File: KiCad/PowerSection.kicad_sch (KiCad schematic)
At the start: 24 parts, among them U2 LM7805_TO220, U4 LM337_TO220, U6 MC34063AP, U7 LM7810_TO220

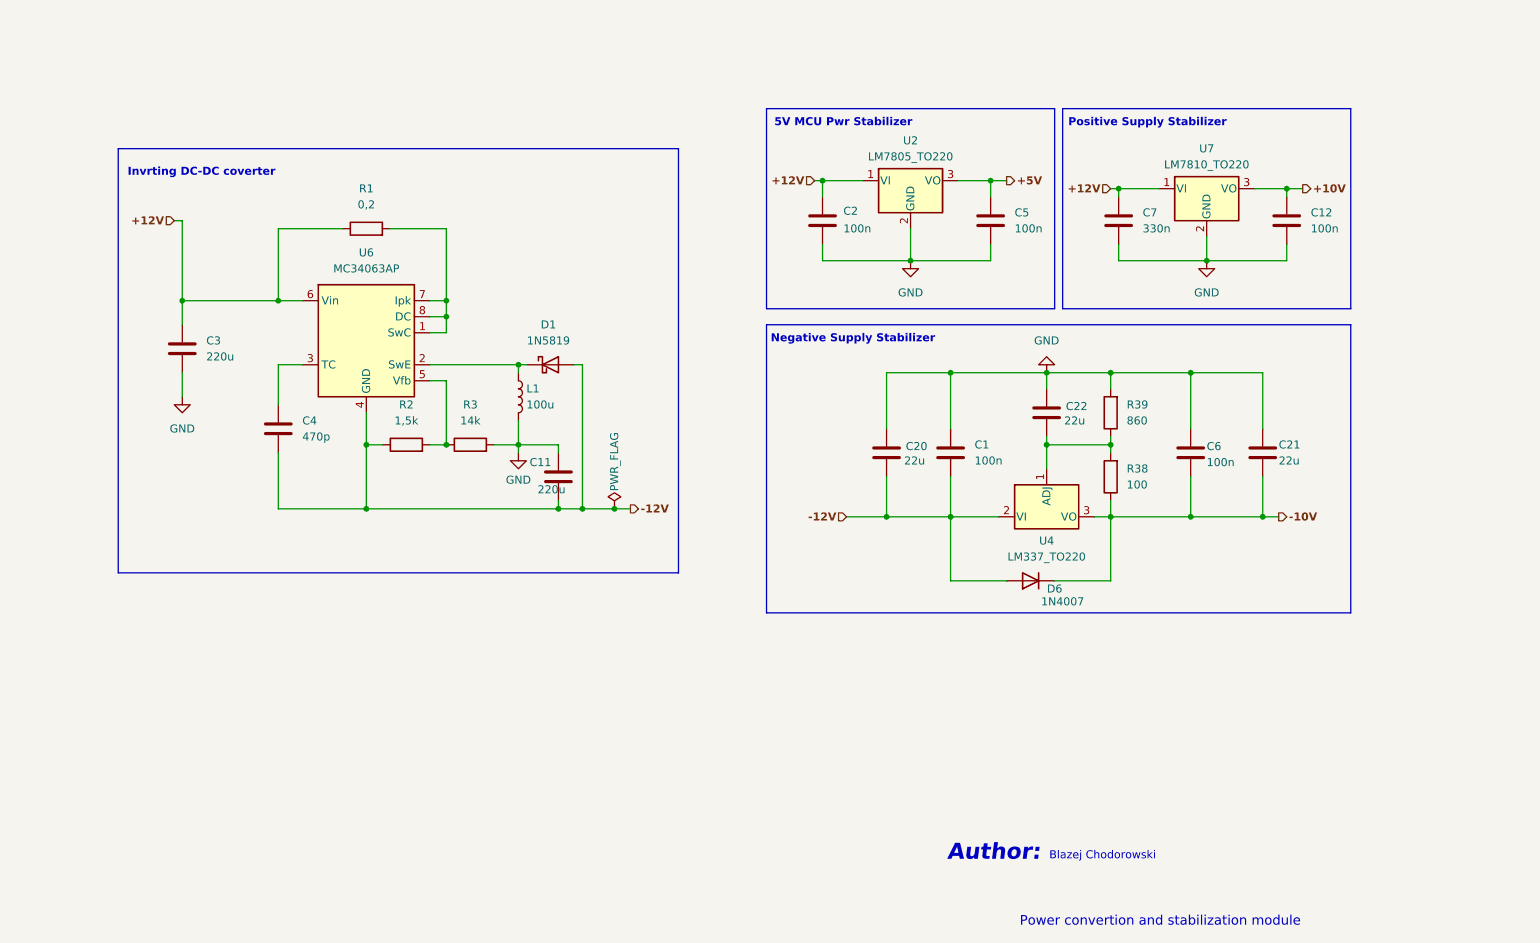
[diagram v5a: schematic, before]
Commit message: First DAC layout, rough board layout
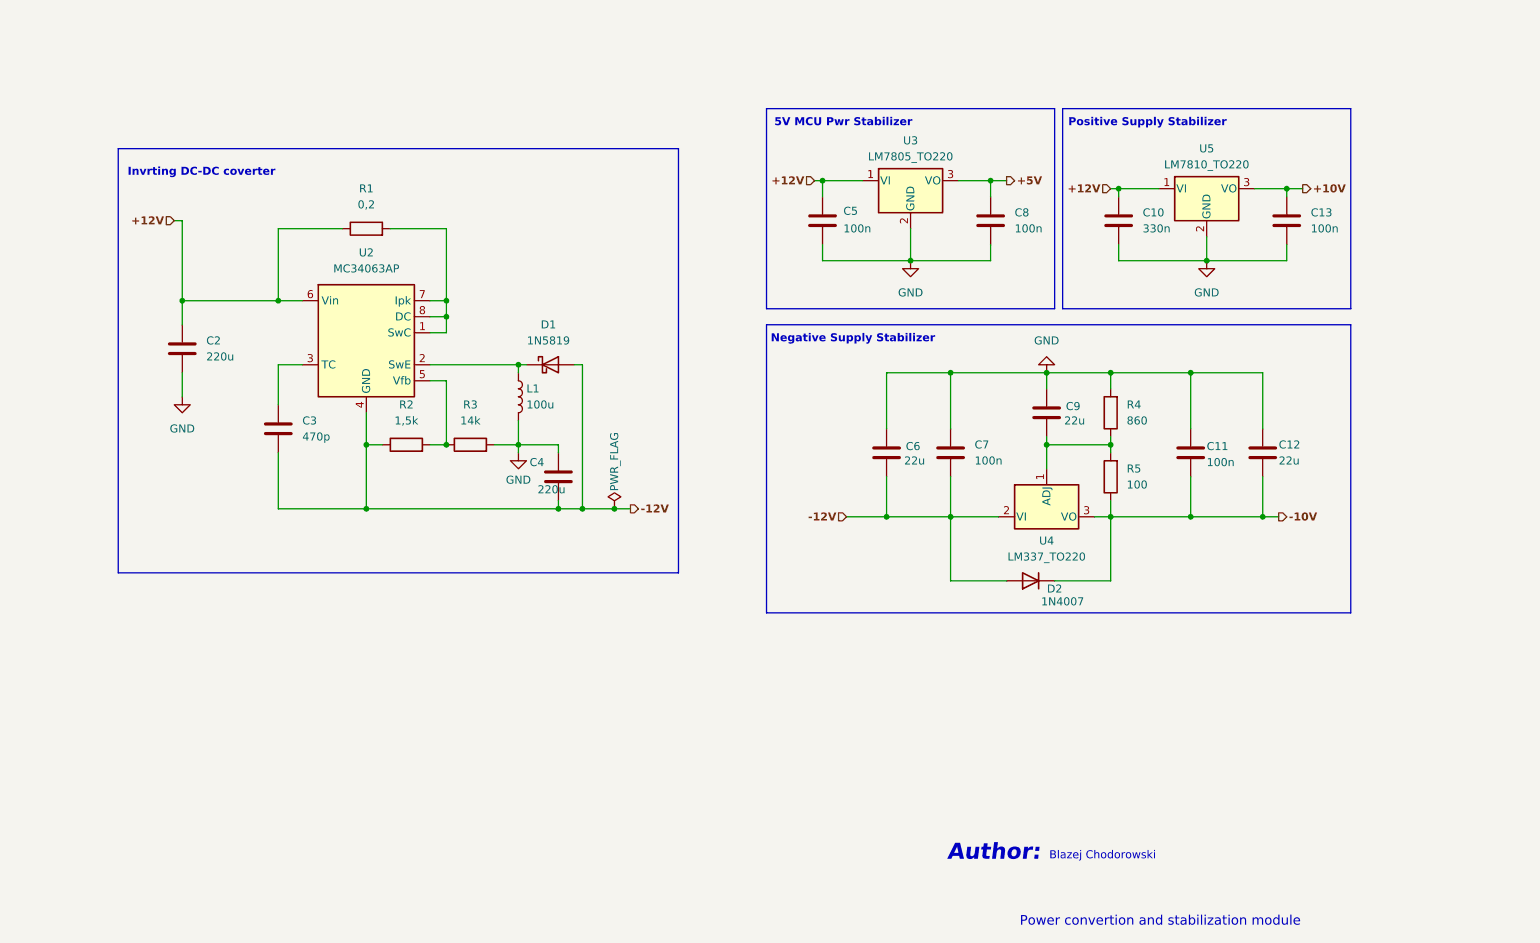
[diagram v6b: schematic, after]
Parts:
- renumbered C7 to C10, C6 to C11, C21 to C12, C12 to C13, C3 to C2, C4 to C3, C11 to C4, C2 to C5, C20 to C6, C1 to C7, C5 to C8, C22 to C9, D6 to D2, R39 to R4, R38 to R5, U6 to U2, U2 to U3, U7 to U5
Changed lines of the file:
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@@
 		(on_board yes)
 		(dnp no)
-		(property "Reference" "C6"
+		(property "Reference" "C11"
 			(at 218.44 114.554 0)
 			(effects
@@
 			(project "SiganlGen"
 				(path "/e2db369b-fed9-4358-b449-15db5155edf2/27026b69-1c54-41be-a6f6-95a262163c29"
-					(reference "C6")
+					(reference "C11")
 					(unit 1)
 				)
@@
 		(dnp no)
 		(fields_autoplaced yes)
-		(property "Reference" "C1"
+		(property "Reference" "C7"
 			(at 181.61 114.2999 0)
 			(effects
@@
 			(project "SiganlGen"
 				(path "/e2db369b-fed9-4358-b449-15db5155edf2/27026b69-1c54-41be-a6f6-95a262163c29"
-					(reference "C1")
+					(reference "C7")
 					(unit 1)
 				)
@@
 		(dnp no)
 		(fields_autoplaced yes)
-		(property "Reference" "R38"
+		(property "Reference" "R5"
 			(at 205.74 118.1099 0)
 			(effects
@@
 			(project "SiganlGen"
 				(path "/e2db369b-fed9-4358-b449-15db5155edf2/27026b69-1c54-41be-a6f6-95a262163c29"
-					(reference "R38")
+					(reference "R5")
 					(unit 1)
 				)
@@
 		(dnp no)
 		(fields_autoplaced yes)
-		(property "Reference" "R39"
+		(property "Reference" "R4"
 			(at 205.74 107.9499 0)
 			(effects
@@
 			(project "SiganlGen"
 				(path "/e2db369b-fed9-4358-b449-15db5155edf2/27026b69-1c54-41be-a6f6-95a262163c29"
-					(reference "R39")
+					(reference "R4")
 					(unit 1)
 				)
@@
 		(dnp no)
 		(fields_autoplaced yes)
-		(property "Reference" "C4"
+		(property "Reference" "C3"
 			(at 74.93 110.4899 0)
 			(effects
@@
 			(project "SiganlGen"
 				(path "/e2db369b-fed9-4358-b449-15db5155edf2/27026b69-1c54-41be-a6f6-95a262163c29"
-					(reference "C4")
+					(reference "C3")
 					(unit 1)
 				)
@@
 		(dnp no)
 		(fields_autoplaced yes)
-		(property "Reference" "U6"
+		(property "Reference" "U2"
 			(at 85.09 83.82 0)
 			(effects
@@
 			(project "SiganlGen"
 				(path "/e2db369b-fed9-4358-b449-15db5155edf2/27026b69-1c54-41be-a6f6-95a262163c29"
-					(reference "U6")
+					(reference "U2")
 					(unit 1)
 				)
@@
 		(dnp no)
 		(fields_autoplaced yes)
-		(property "Reference" "C7"
+		(property "Reference" "C10"
 			(at 208.28 77.4699 0)
 			(effects
@@
 			(project "SiganlGen"
 				(path "/e2db369b-fed9-4358-b449-15db5155edf2/27026b69-1c54-41be-a6f6-95a262163c29"
-					(reference "C7")
+					(reference "C10")
 					(unit 1)
 				)
@@
 		(dnp no)
 		(fields_autoplaced yes)
-		(property "Reference" "C5"
+		(property "Reference" "C8"
 			(at 187.96 77.4699 0)
 			(effects
@@
 			(project "SiganlGen"
 				(path "/e2db369b-fed9-4358-b449-15db5155edf2/27026b69-1c54-41be-a6f6-95a262163c29"
-					(reference "C5")
+					(reference "C8")
 					(unit 1)
 				)
@@
 		(dnp no)
 		(fields_autoplaced yes)
-		(property "Reference" "U2"
+		(property "Reference" "U3"
 			(at 171.45 66.04 0)
 			(effects
@@
 			(project "SiganlGen"
 				(path "/e2db369b-fed9-4358-b449-15db5155edf2/27026b69-1c54-41be-a6f6-95a262163c29"
-					(reference "U2")
+					(reference "U3")
 					(unit 1)
 				)
@@
 		(dnp no)
 		(fields_autoplaced yes)
-		(property "Reference" "C3"
+		(property "Reference" "C2"
 			(at 59.69 97.7899 0)
 			(effects
@@
 			(project "SiganlGen"
 				(path "/e2db369b-fed9-4358-b449-15db5155edf2/27026b69-1c54-41be-a6f6-95a262163c29"
-					(reference "C3")
+					(reference "C2")
 					(unit 1)
 				)
@@
 		(dnp no)
 		(fields_autoplaced yes)
-		(property "Reference" "C12"
+		(property "Reference" "C13"
 			(at 234.95 77.4699 0)
 			(effects
@@
 			(project "SiganlGen"
 				(path "/e2db369b-fed9-4358-b449-15db5155edf2/27026b69-1c54-41be-a6f6-95a262163c29"
-					(reference "C12")
+					(reference "C13")
 					(unit 1)
 				)
@@
 		(on_board yes)
 		(dnp no)
-		(property "Reference" "C2"
+		(property "Reference" "C5"
 			(at 160.782 77.216 0)
 			(effects
@@
 			(project "SiganlGen"
 				(path "/e2db369b-fed9-4358-b449-15db5155edf2/27026b69-1c54-41be-a6f6-95a262163c29"
-					(reference "C2")
+					(reference "C5")
 					(unit 1)
 				)
@@
 		(dnp no)
 		(fields_autoplaced yes)
-		(property "Reference" "U7"
+		(property "Reference" "U5"
 			(at 218.44 67.31 0)
 			(effects
@@
 			(project "SiganlGen"
 				(path "/e2db369b-fed9-4358-b449-15db5155edf2/27026b69-1c54-41be-a6f6-95a262163c29"
-					(reference "U7")
+					(reference "U5")
 					(unit 1)
 				)
@@
 		(on_board yes)
 		(dnp no)
-		(property "Reference" "D6"
+		(property "Reference" "D2"
 			(at 194.31 137.16 0)
 			(effects
@@
 			(project "SiganlGen"
 				(path "/e2db369b-fed9-4358-b449-15db5155edf2/27026b69-1c54-41be-a6f6-95a262163c29"
-					(reference "D6")
+					(reference "D2")
 					(unit 1)
 				)
@@
 		(on_board yes)
 		(dnp no)
-		(property "Reference" "C20"
+		(property "Reference" "C6"
 			(at 170.688 114.554 0)
 			(effects
@@
 			(project "SiganlGen"
 				(path "/e2db369b-fed9-4358-b449-15db5155edf2/27026b69-1c54-41be-a6f6-95a262163c29"
-					(reference "C20")
+					(reference "C6")
 					(unit 1)
 				)
@@
 		(on_board yes)
 		(dnp no)
-		(property "Reference" "C11"
+		(property "Reference" "C4"
 			(at 110.998 117.094 0)
 			(effects
@@
 			(project "SiganlGen"
 				(path "/e2db369b-fed9-4358-b449-15db5155edf2/27026b69-1c54-41be-a6f6-95a262163c29"
-					(reference "C11")
+					(reference "C4")
 					(unit 1)
 				)
@@
 		(on_board yes)
 		(dnp no)
-		(property "Reference" "C21"
+		(property "Reference" "C12"
 			(at 229.87 114.3 0)
 			(effects
@@
 			(project "SiganlGen"
 				(path "/e2db369b-fed9-4358-b449-15db5155edf2/27026b69-1c54-41be-a6f6-95a262163c29"
-					(reference "C21")
+					(reference "C12")
 					(unit 1)
 				)
@@
 		(on_board yes)
 		(dnp no)
-		(property "Reference" "C22"
+		(property "Reference" "C9"
 			(at 196.088 108.204 0)
 			(effects
@@
 			(project "SiganlGen"
 				(path "/e2db369b-fed9-4358-b449-15db5155edf2/27026b69-1c54-41be-a6f6-95a262163c29"
-					(reference "C22")
-					(unit 1)
-				)
+					(reference "C9")
+					(unit 1)
+				)

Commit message: bom, changed lm7810 to lm317
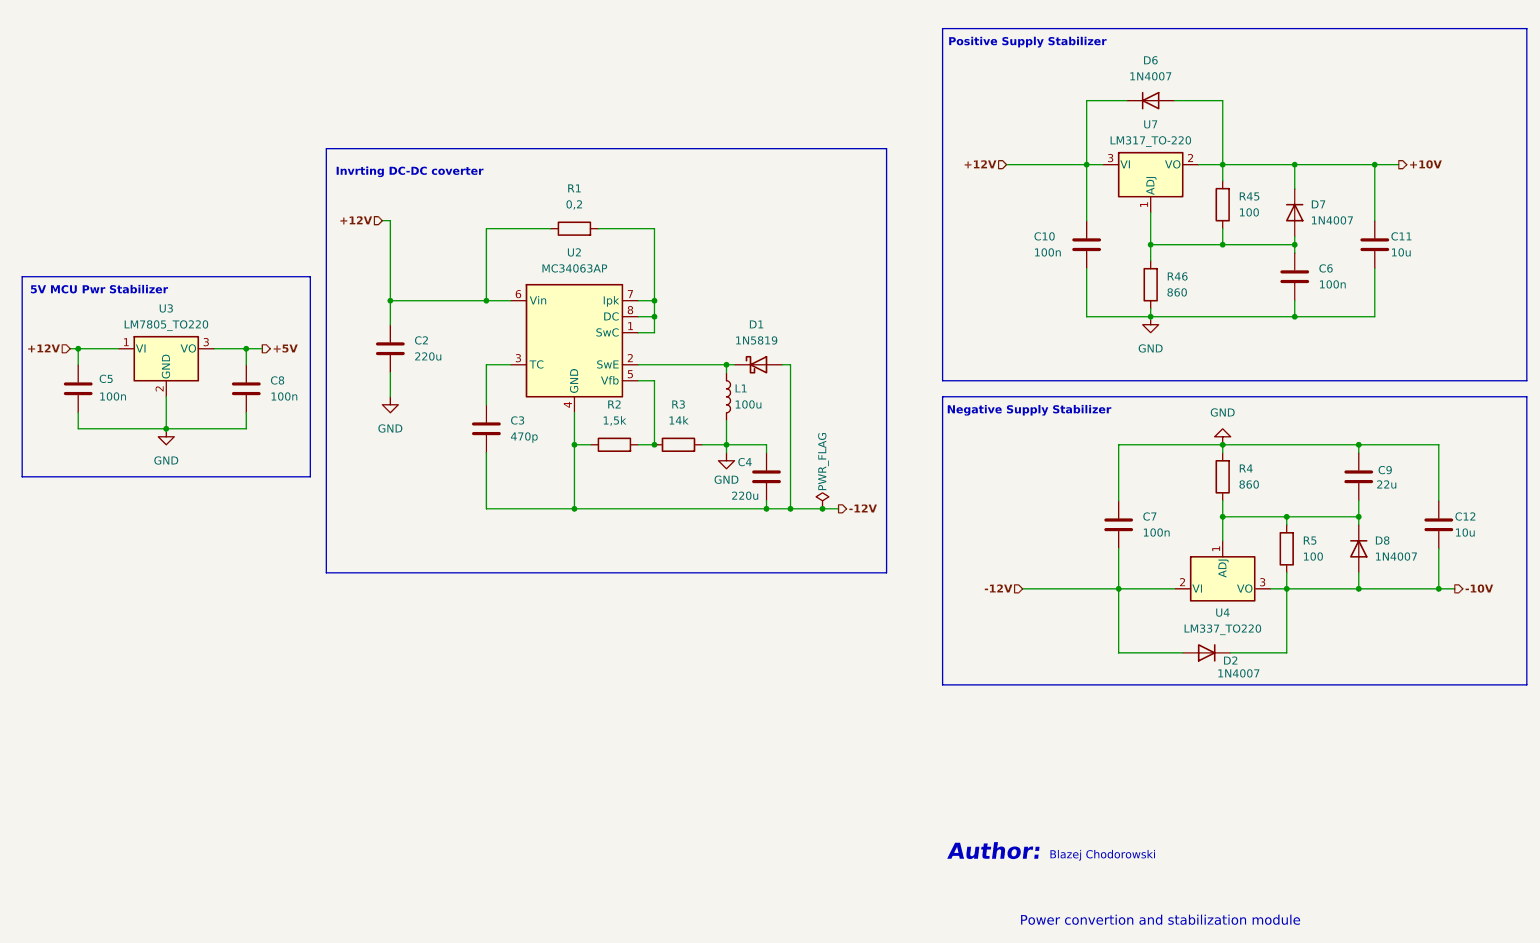
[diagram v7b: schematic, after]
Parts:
- removed C13: 100n, Capacitor_SMD:C_0805_2012Metric_Pad1.18x1.45mm_HandSolder, symbol Device:C
- removed U5: LM7810_TO220, Package_TO_SOT_THT:TO-220-3_Vertical, symbol Regulator_Linear:LM7810_TO220
- added D6, D7, D8: 1N4007, Diode_SMD:D_SOD-123F, symbol Diode:1N4007
- added R45: 100, Resistor_SMD:R_0805_2012Metric_Pad1.20x1.40mm_HandSolder, symbol Device:R
- added R46: 860, Resistor_SMD:R_0805_2012Metric_Pad1.20x1.40mm_HandSolder, symbol Device:R
- added U7: LM317_TO-220, Package_TO_SOT_THT:TO-220-3_Vertical, symbol Regulator_Linear:LM317_TO-220
- C10: value 330n -> 100n
- C11: value 100n -> 10u; footprint Capacitor_SMD:C_0805_2012Metric_Pad1.18x1.45mm_HandSolder -> Capacitor_SMD:CP_Elec_6.3x5.3
- C12: value 22u -> 10u
- C6: value 22u -> 100n; footprint Capacitor_SMD:CP_Elec_6.3x5.3 -> Capacitor_SMD:C_0805_2012Metric_Pad1.18x1.45mm_HandSolder
- D2: footprint Diode_THT:D_DO-41_SOD81_P10.16mm_Horizontal -> Diode_SMD:D_SOD-123F
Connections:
- net +10V: now also C11.1, D6.2 (A), D7.1 (K), R45.2, U7.2 (VO)
- net +12V: now also D6.1 (K), U7.3 (VI)
- net -10V: now also D8.2 (A); no longer C11.2
- net -12V: no longer C6.2
- net GND: now also C11.2, C6.2, R46.1; no longer C11.1, C6.1
- net at C9.2, R4.1, R5.2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: now also D8.1 (K)
- new net: C6.1, D7.2 (A), R45.1, R46.2, U7.1 (ADJ)
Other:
- moved on the sheet: C12, C2, C3, C4, C5, C7, C8, C9, D1, D2, L1, R1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

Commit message: Changed stabilizator capacitors values
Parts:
- C11, C12: value 10u -> 22u
- C6: value 100n -> 22u
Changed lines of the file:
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@@
 			)
 		)
-		(property "Value" "100n"
+		(property "Value" "22u"
 			(at 236.22 88.8999 0)
 			(effects
@@
 			)
 		)
-		(property "Value" "10u"
+		(property "Value" "22u"
 			(at 247.65 83.82 0)
 			(effects
@@
 			)
 		)
-		(property "Value" "10u"
+		(property "Value" "22u"
 			(at 257.81 128.27 0)
 			(effects
